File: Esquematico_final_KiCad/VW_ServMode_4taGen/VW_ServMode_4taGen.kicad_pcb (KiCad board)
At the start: 2 copper layers, 90 x 55 mm, 96 parts, among them J1 Conn_02x03_Counter_Clockwise, J10 Micro_SD_Card, J11 USB_C_Receptacle_USB2.0_14P, J12 Conn_02x04_Counter_Clockwise, J2 Conn_01x04_Pin, J3 Conn_01x02_Pin, J4 Conn_01x02_Pin, J5 Conn_01x02_Pin, J6 Conn_01x02_Pin, J7 Conn_01x02_Pin, Q1 IRLML6402, SW1 SW_In, SW2 SW_Out, SW4 SW_Out, U1 TP4056, U2 DW01, U3 FS8205A, U4 AMS1117-3.3, U5 STM32F103C6Tx, Y1 Crystal

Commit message: - BOM actualizado - Gerbers generados
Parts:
- D2: value BAT25 -> D_OK
- D3: value BAT50 -> D_ERR
- D4: value BAT75 -> D_MSON
- D5: value BAT99 -> D_MSOFF
- R26: value R5K -> R5K1
- U3: footprint Package_SO:TSSOP-8_4.4x3mm_P0.65mm -> Package_TO_SOT_SMD:SOT-23-6_Handsoldering
- U5: value STM32F103C6Tx -> STM32F103C8T6
- moved R13 1.70 mm to (198.1, 29.7), turned to 0 degrees
- moved R12 1.70 mm to (198.1, 28.0), turned to 0 degrees
- moved U3 0.50 mm to (202.6, 51.4)
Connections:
- J12 pad 2: unconnected-(J12-Pin_2-Pad2) -> DO_3V3
- J12 pad 4: GND -> unconnected-(J12-Pin_4-Pad4)
- J12 pad 5: CONN_SDA -> unconnected-(J12-Pin_5-Pad5)
- J12 pad 7: unconnected-(J12-Pin_7-Pad7) -> GND
- J12 pad 8: DO_3V3 -> CONN_SDA
- R6 pad 1: Net-(R6-Pad1) -> GND
- U3 pad 1: unconnected-(U3-D12-Pad1) -> TP_B-
- U3 pad 2: TP_B- -> unconnected-(U3-D12-Pad2)
- U3 pad 3: TP_B- -> GND
- U3 pad 4: Net-(U2-OD) -> Net-(U2-OC)
- U3 pad 5: Net-(U2-OC) -> unconnected-(U3-D12-Pad5)
- U3 pad 6: Net-(R6-Pad1) -> Net-(U2-OD)
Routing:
- net Net-(R6-Pad1): track 11.8 -> 0.00 mm
- net DO_3V3: track 30.8 -> 39.8 mm
- net CONN_SDA: track 62.2 -> 54.8 mm
- net Net-(U2-OD): track 6.53 -> 13.2 mm
- net CONN_SCL: track 57.2 -> 52.5 mm
- net unconnected-(U5-PB5-Pad41): track 0.00 -> 3.67 mm, vias 0 -> 1
- net TP_B-: track 88.1 -> 84.7 mm
- net unconnected-(U5-PA15-Pad38): track 0.00 -> 2.57 mm, vias 0 -> 1
- net Net-(U2-OC): track 9.52 -> 8.44 mm
- net DCLK: track 40.7 -> 39.8 mm
- net LED_OK: track 39.6 -> 39.1 mm
- net GND: vias 44 -> 45
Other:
- board text added: "0"
- board text added: "1"
- board text added: "BOOT0"
- board text added: "BOOT1"

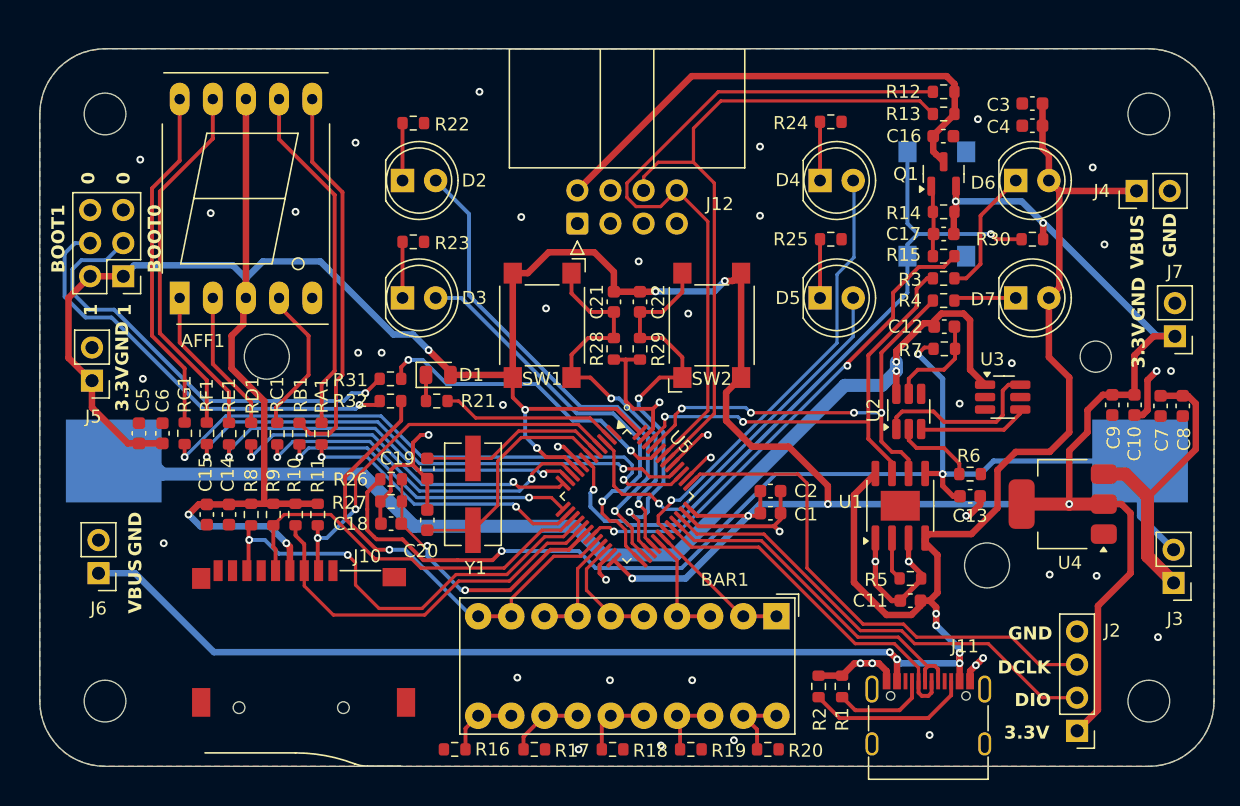
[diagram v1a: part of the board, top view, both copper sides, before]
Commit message: Errores corregidos - Resistencias en bus usb, leds cerca de usb, leds de nivel de batería
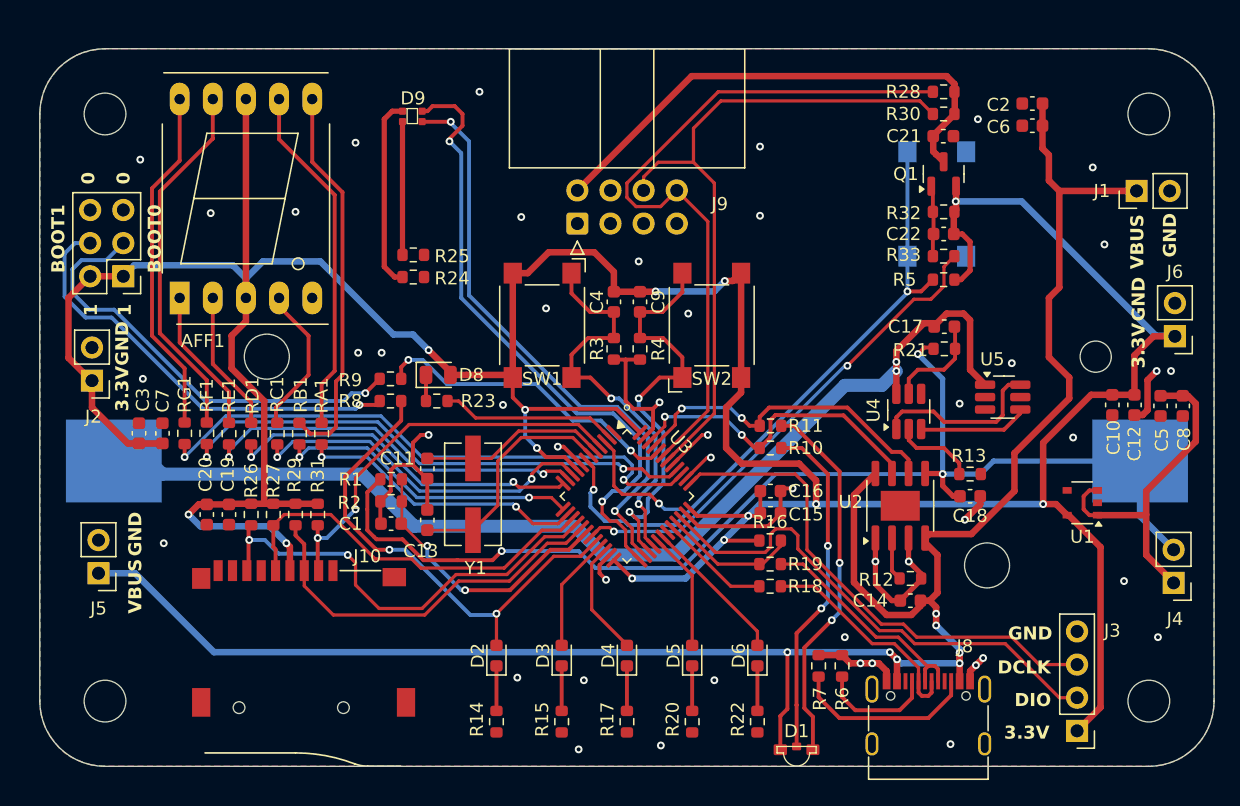
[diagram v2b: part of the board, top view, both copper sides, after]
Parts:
- removed BAR1: HDSP-4830_2, Display:HDSP-4830
- removed D7: LED, LED_THT:LED_D5.0mm
- removed the R24 at (189.4, 30.3)
- removed the R25 at (189.4, 39.3)
- removed the U4 at (207.2, 59.6)
- added D1: DUAL LED, JCU_LED_SMD:1204 DUAL LED, F.Cu at (186.8, 78.2)
- added D9: LED_Dual_KAKA, JCU_LED_SMD:0805 DUAL LED, F.Cu at (156.8, 29.3)
- added R16: R1K5, Resistor_SMD:R_0603_1608Metric, F.Cu at (184.8, 62.4)
- added R18: R22, Resistor_SMD:R_0603_1608Metric, F.Cu at (184.8, 65.9)
- added R19: R22, Resistor_SMD:R_0603_1608Metric, F.Cu at (184.8, 64.2)
- added U1: ~, Package_SO:TSOP-5_1.65x3.05mm_P0.95mm, F.Cu at (208.7, 59.5)
- D2: value D_OK -> BAT00; footprint LED_THT:LED_D5.0mm -> LED_SMD:LED_0603_1608Metric
- D3: value D_ERR -> BAT25; footprint LED_THT:LED_D5.0mm -> LED_SMD:LED_0603_1608Metric
- D4: value D_MSON -> BAT50; footprint LED_THT:LED_D5.0mm -> LED_SMD:LED_0603_1608Metric
- D5: value D_MSOFF -> BAT75; footprint LED_THT:LED_D5.0mm -> LED_SMD:LED_0603_1608Metric
- D6: value LED -> BAT100; footprint LED_THT:LED_D5.0mm -> LED_SMD:LED_0603_1608Metric
- SW3: renamed from SW4; value SW_Out -> SW_RST
- moved D6 41.4 mm to (183.8, 71.2), turned to 90 degrees
- moved D4 39.3 mm to (173.8, 71.2), turned to 90 degrees
- moved D2 37.1 mm to (163.8, 71.2), turned to 90 degrees
- moved D3 30.0 mm to (168.8, 71.2), turned to 90 degrees
- moved D5 29.1 mm to (178.8, 71.2), turned to 90 degrees
- moved R10 18.6 mm to (184.8, 55.3)
- moved R11 16.4 mm to (184.8, 53.6)
- moved R24 11.8 mm to (157.4, 42.2)
- moved R5 7.47 mm to (198.1, 42.4)
- moved R14 3.84 mm to (163.8, 76.3), turned to -90 degrees
- moved R15 2.99 mm to (168.8, 76.3), turned to -90 degrees
- moved R17 2.39 mm to (173.8, 76.3), turned to -90 degrees
- moved R22 2.27 mm to (183.8, 76.3), turned to -90 degrees
- moved R20 2.13 mm to (178.8, 76.3), turned to -90 degrees
- moved R6 1.58 mm to (190.3, 72.0)
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- renumbered C18 to C1, C9 to C10, C19 to C11, C10 to C12, C20 to C13, C11 to C14, C1 to C15, C2 to C16, C12 to C17, C13 to C18, C14 to C19, C3 to C2, C15 to C20, C16 to C21, C17 to C22, C5 to C3, C21 to C4, C7 to C5, C4 to C6, C6 to C7, C22 to C9, D1 to D8, J4 to J1, J5 to J2, J2 to J3, J3 to J4, J6 to J5, J7 to J6, J1 to J7, J11 to J8, J12 to J9, R26 to R1, R3 to R10, R4 to R11, R5 to R12, R6 to R13, R16 to R14, R17 to R15, R18 to R17, R27 to R2, R19 to R20, R7 to R21, R20 to R22, R21 to R23, R22 to R24, R23 to R25, R8 to R26, R9 to R27, R12 to R28, R10 to R29, R28 to R3, R13 to R30, R11 to R31, R14 to R32, R15 to R33, R29 to R4, R30 to R5, R1 to R6, R2 to R7, R32 to R8, R31 to R9, U1 to U2, U5 to U3, U2 to U4, U3 to U5
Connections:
- BT1 pad 1: BAT+ -> Net-(BT1-+)
- D2 pad 2: LED_OK -> LED_B00
- D3 pad 2: LED_ERROR -> LED_B25
- D4 pad 2: LED_MODSERV_ON -> LED_B50
- D5 pad 2: LED_MODSERV_OFF -> LED_B75
- D6 pad 2: TP_IN -> LED_B99
- R10 pad 2: Net-(D6-K) -> Net-(D1-G)
- R14 pad 1: Net-(BAR1-K-Pad11) -> Net-(D2-K)
- R15 pad 1: Net-(BAR1-K-Pad13) -> Net-(D3-K)
- R17 pad 1: Net-(BAR1-K-Pad15) -> Net-(D4-K)
- R20 pad 1: Net-(BAR1-K-Pad17) -> Net-(D5-K)
- R22 pad 1: Net-(BAR1-K-Pad19) -> Net-(D6-K)
- R24 pad 1: Net-(D2-K) -> Net-(D9-K1)
- R25 pad 1: Net-(D3-K) -> Net-(D9-K2)
- U3 pad 3: LED_MODSERV_OFF -> unconnected-(U3-PC14-Pad3)
- U3 pad 31: LED_MODSERV_ON -> unconnected-(U3-PA10-Pad31)
- U3 pad 32: USB_D- -> Net-(U3-PA11)
- U3 pad 33: USB_D+ -> Net-(U3-PA12)
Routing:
- net LED_MODSERV_ON: track 33.9 -> 0.00 mm, vias 1 -> 0
- net LED_MODSERV_OFF: track 31.2 -> 0.00 mm, vias 1 -> 0
- net Net-(D1-G): track 0.00 -> 26.0 mm, vias 0 -> 2
- net Net-(D1-R): track 4.78 -> 28.3 mm, vias 0 -> 2
- net LED_ERROR: track 32.6 -> 49.0 mm, vias 1 -> 2
- net Net-(D9-K1): track 0.00 -> 14.7 mm
- net TP_#CHRG: track 36.2 -> 24.9 mm
- net Net-(U3-PA12): track 0.00 -> 10.3 mm
- net Net-(D9-K2): track 0.00 -> 10.2 mm
- net USB_D-: track 27.3 -> 17.2 mm
- net TP_#STDBY: track 35.4 -> 25.5 mm, vias 4 -> 2
- net unconnected-(U3-PC14-Pad3): track 0.00 -> 9.52 mm, vias 0 -> 1
- net USB_D+: track 26.9 -> 17.6 mm
- net Net-(U3-PA11): track 0.00 -> 8.58 mm
- net Net-(D6-K): track 9.97 -> 3.45 mm
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
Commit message: Segunda version finalizada
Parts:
- removed D9: LED_Dual_KAKA, JCU_LED_SMD:0805 DUAL LED
- added D7: ~, JCU_LED_SMD:SMD-4P,3.5x2.8mm, F.Cu at (155.0, 35.5)
- D1: value DUAL LED -> ~; footprint JCU_LED_SMD:1204 DUAL LED -> JCU_LED_SMD:SMD,2x3mm
- D2, D3, D4, D5, D6: footprint LED_SMD:LED_0603_1608Metric -> LED_THT:LED_Rectangular_W5.0mm_H2.0mm
- moved C2 36.9 mm to (207.0, 65.7), turned to 180 degrees
- moved C6 33.5 mm to (207.0, 64.0), turned to 180 degrees
- moved D1 17.7 mm to (204.5, 78.2)
- moved C21 8.62 mm to (191.0, 36.4)
- moved R30 8.62 mm to (191.1, 34.7)
- moved C22 8.62 mm to (191.1, 43.9)
- moved Q1 8.62 mm to (191.1, 39.3)
- moved R28 8.62 mm to (191.1, 33.0)
- moved R32 8.62 mm to (191.1, 42.2)
- moved R33 8.62 mm to (191.1, 45.6)
- moved R5 8.62 mm to (191.1, 47.4)
- moved R24 5.11 mm to (155.7, 47.0), turned to 180 degrees
- moved R25 5.11 mm to (155.7, 45.3), turned to 180 degrees
- moved D2 4.36 mm to (167.8, 72.9)
- moved D6 4.36 mm to (179.8, 72.9)
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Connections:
- BT1 pad 1: Net-(BT1-+) -> BAT+
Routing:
- net CONN_SCL: track 52.5 -> 39.5 mm
- net +3V3: track 298.9 -> 287.6 mm
- net DO_3V3: track 39.8 -> 30.8 mm
- net Net-(D1-B): track 28.3 -> 37.0 mm
- net Net-(D1-R): track 26.0 -> 34.3 mm
- net DO_CONTROL3V3: track 37.9 -> 29.7 mm
- net CONN_SDA: track 54.8 -> 46.9 mm
- net LED_OK: track 45.3 -> 39.9 mm
- net PUSH_IN: track 30.7 -> 35.6 mm
- net PUSH_OUT: track 32.1 -> 36.6 mm
- net Net-(U4-VCC): track 8.12 -> 3.84 mm
- net Net-(D7-KR): track 14.7 -> 10.8 mm
- net GND: track 66.9 -> 70.4 mm, vias 45 -> 49
- net USB_D+: track 17.6 -> 14.6 mm
- net DIO: track 38.7 -> 36.0 mm
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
